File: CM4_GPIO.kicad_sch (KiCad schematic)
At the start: 13 parts, among them J10 Conn_01x03, J4 THD-20-R, J9 Conn_01x03, U12 SI-51005-F, U2 74LVC1G07SE-7

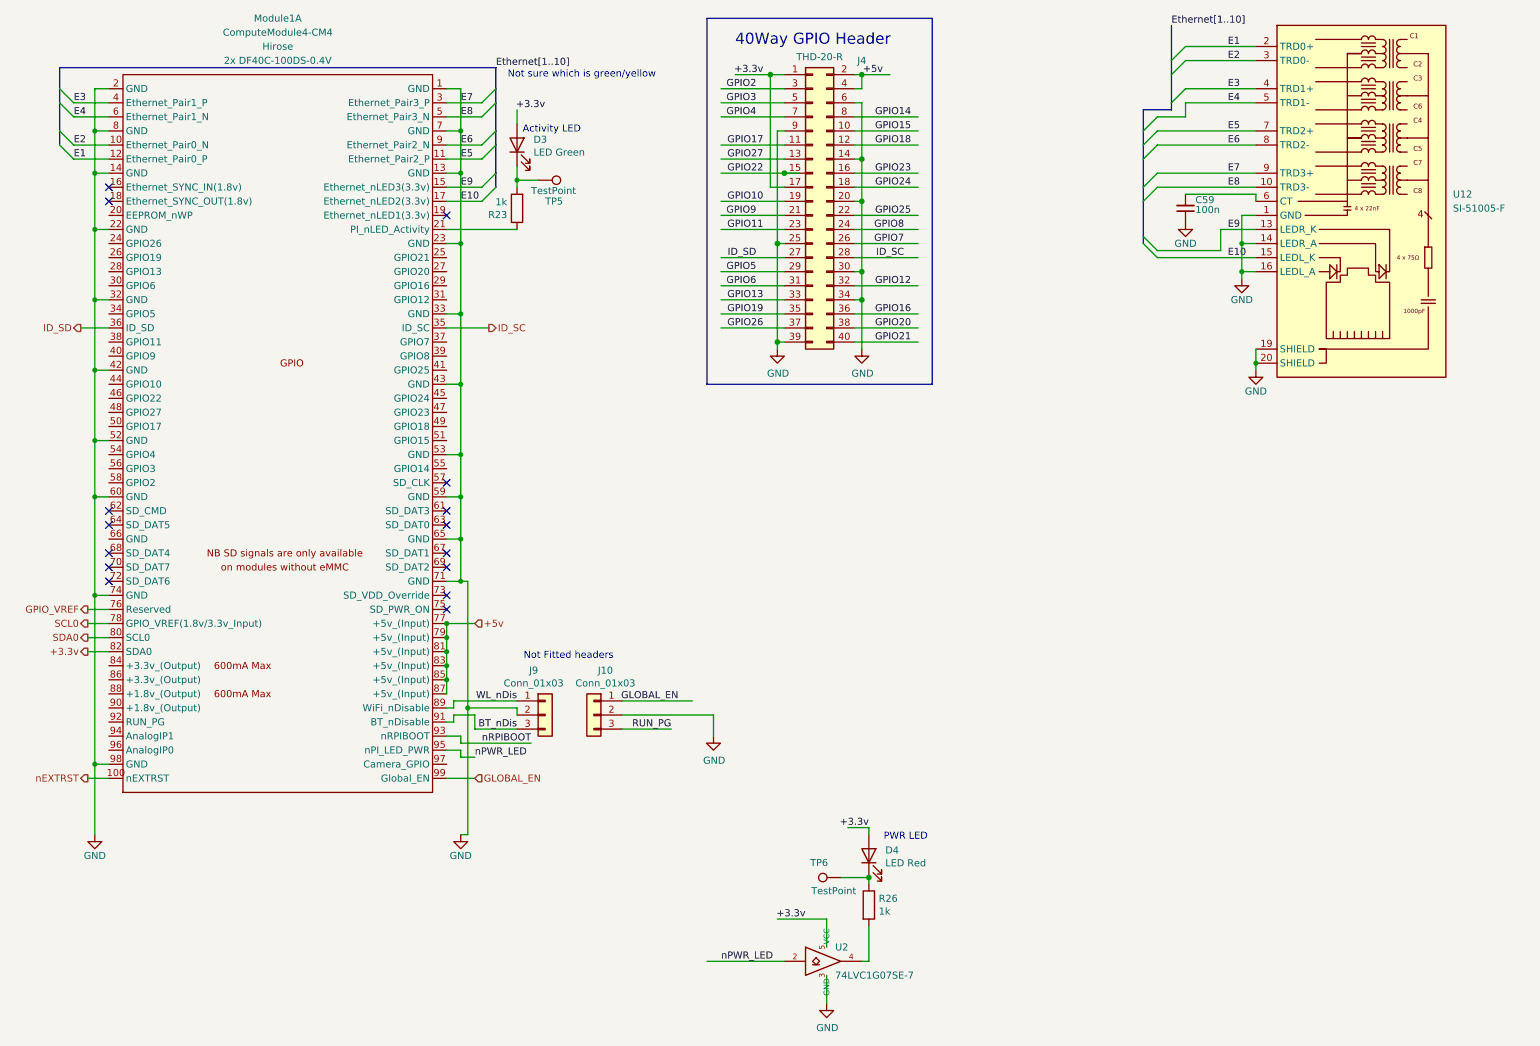
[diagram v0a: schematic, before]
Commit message: Heb mijn documentatie geleverd voor de USB-c en heb een BOM toegevoegd
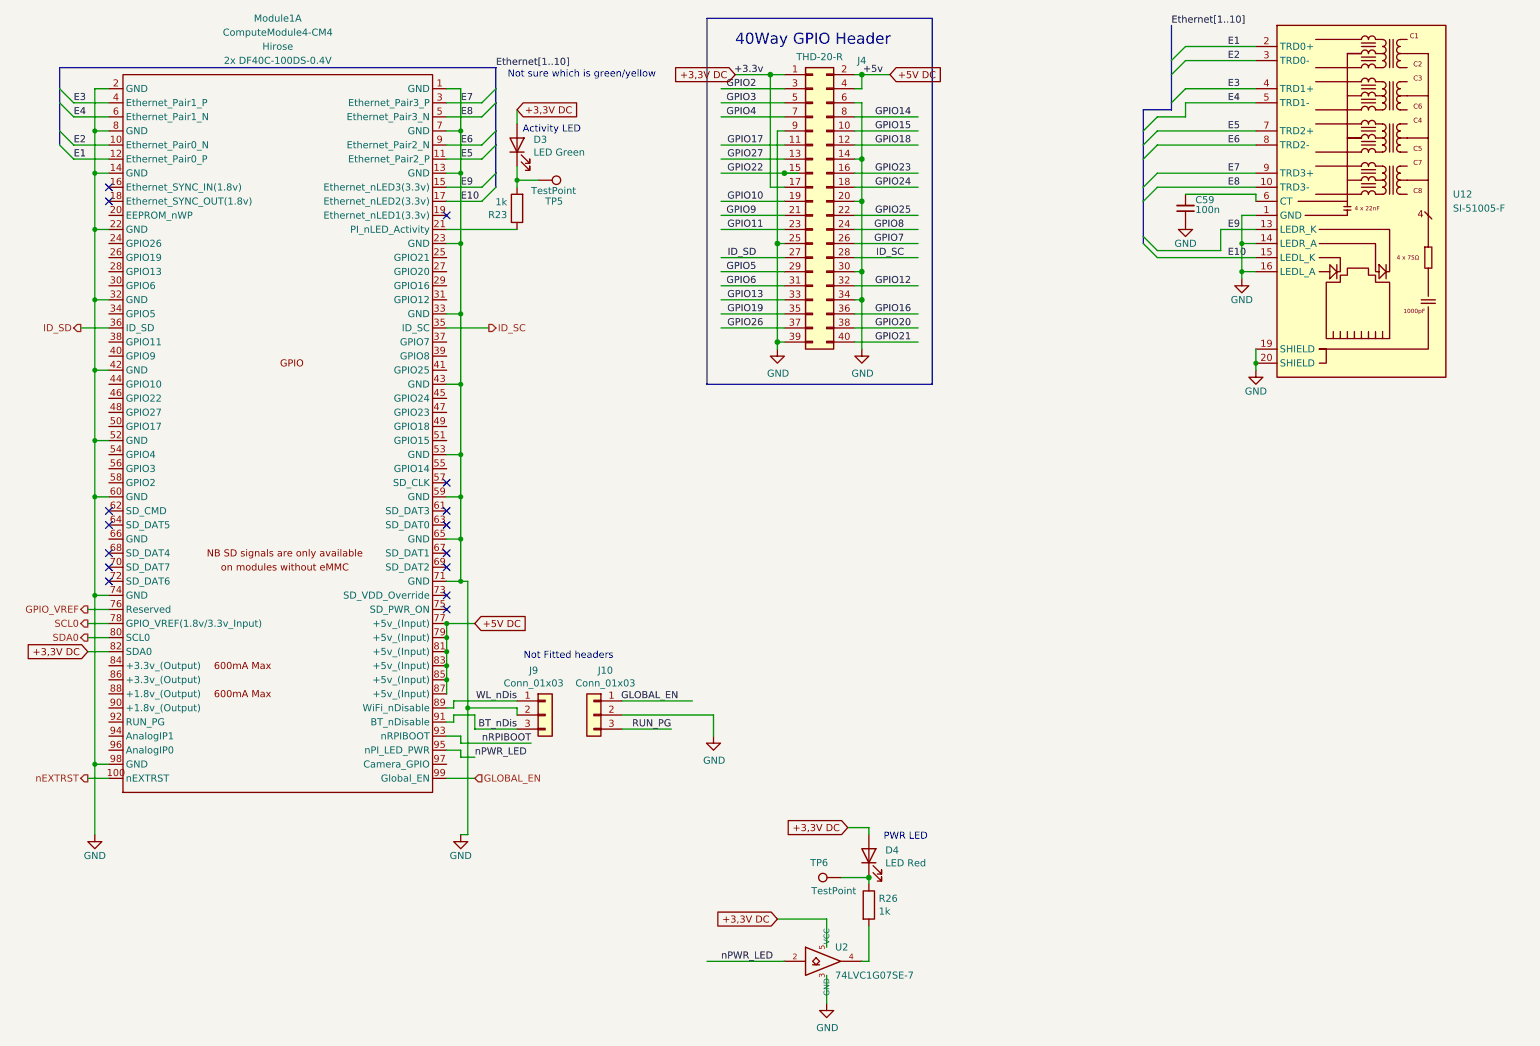
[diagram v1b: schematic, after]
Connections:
- net +3.3v is gone; now on net +3,3V DC: D4.2 (A), J4.1 (Pin_1), J4.17 (Pin_17), Module1.82 (SDA0), U2.5 (VCC)
- net +3,3V DC: now reaches D3.2 (A)
- net +5v renamed +5V DC
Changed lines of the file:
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@@
-		)
-	)
-	(label "+3.3v"
-		(at 153.67 176.53 180)
-		(effects
-			(font
-				(size 1.27 1.27)
-			)
-			(justify right bottom)
 		)
 	)
@@
 		)
 	)
-	(label "+3.3v"
-		(at 165.1 160.02 180)
-		(effects
-			(font
-				(size 1.27 1.27)
-			)
-			(justify right bottom)
-		)
-	)
 	(label "GPIO20"
 		(at 172.72 69.85 180)
@@
 		)
 	)
-	(label "+3.3v"
-		(at 106.68 30.48 180)
-		(effects
-			(font
-				(size 1.27 1.27)
-			)
-			(justify right bottom)
-		)
-	)
 	(label "E4"
 		(at 229.87 29.21 0)
@@
 			)
 			(justify right bottom)
+		)
+	)
+	(global_label "+5V DC"
+		(shape input)
+		(at 93.98 123.19 0)
+		(fields_autoplaced yes)
+		(effects
+			(font
+				(size 1.27 1.27)
+			)
+			(justify left)
+		)
+		(property "Intersheetrefs" "${INTERSHEET_REFS}"
+			(at 104.3433 123.19 0)
+			(effects
+				(font
+					(size 1.27 1.27)
+				)
+				(justify left)
+				(hide yes)
+			)
+		)
+	)
+	(global_label "+3,3V DC"
+		(shape input)
+		(at 161.29 160.02 180)
+		(fields_autoplaced yes)
+		(effects
+			(font
+				(size 1.27 1.27)
+			)
+			(justify right)
+		)
+		(property "Intersheetrefs" "${INTERSHEET_REFS}"
+			(at 149.1124 160.02 0)
+			(effects
+				(font
+					(size 1.27 1.27)
+				)
+				(justify right)
+				(hide yes)
+			)
+		)
+	)
+	(global_label "+3,3V DC"
+		(shape input)
+		(at 148.59 176.53 180)
+		(fields_autoplaced yes)
+		(effects
+			(font
+				(size 1.27 1.27)
+			)
+			(justify right)
+		)
+		(property "Intersheetrefs" "${INTERSHEET_REFS}"
+			(at 136.4124 176.53 0)
+			(effects
+				(font
+					(size 1.27 1.27)
+				)
+				(justify right)
+				(hide yes)
+			)
+		)
+	)
+	(global_label "+5V DC"
+		(shape input)
+		(at 168.91 24.13 0)
+		(fields_autoplaced yes)
+		(effects
+			(font
+				(size 1.27 1.27)
+			)
+			(justify left)
+		)
+		(property "Intersheetrefs" "${INTERSHEET_REFS}"
+			(at 179.2733 24.13 0)
+			(effects
+				(font
+					(size 1.27 1.27)
+				)
+				(justify left)
+				(hide yes)
+			)
+		)
+	)
+	(global_label "+3,3V DC"
+		(shape input)
+		(at 24.13 128.27 180)
+		(fields_autoplaced yes)
+		(effects
+			(font
+				(size 1.27 1.27)
+			)
+			(justify right)
+		)
+		(property "Intersheetrefs" "${INTERSHEET_REFS}"
+			(at 11.9524 128.27 0)
+			(effects
+				(font
+					(size 1.27 1.27)
+				)
+				(justify right)
+				(hide yes)
+			)
+		)
+	)
+	(global_label "+3,3V DC"
+		(shape input)
+		(at 140.97 24.13 180)
+		(fields_autoplaced yes)
+		(effects
+			(font
+				(size 1.27 1.27)
+			)
+			(justify right)
+		)
+		(property "Intersheetrefs" "${INTERSHEET_REFS}"
+			(at 128.7924 24.13 0)
+			(effects
+				(font
+					(size 1.27 1.27)
+				)
+				(justify right)
+				(hide yes)
+			)
+		)
+	)
+	(global_label "+3,3V DC"
+		(shape input)
+		(at 101.6 30.48 0)
+		(fields_autoplaced yes)
+		(effects
+			(font
+				(size 1.27 1.27)
+			)
+			(justify left)
+		)
+		(property "Intersheetrefs" "${INTERSHEET_REFS}"
+			(at 113.7776 30.48 0)
+			(effects
+				(font
+					(size 1.27 1.27)
+				)
+				(justify left)
+				(hide yes)
+			)
 		)
 	)
@@
 		)
 	)
-	(hierarchical_label "+3.3v"
-		(shape output)
-		(at 24.13 128.27 180)
-		(effects
-			(font
-				(size 1.27 1.27)
-			)
-			(justify right)
-		)
-	)
-	(hierarchical_label "+5v"
-		(shape input)
-		(at 93.98 123.19 0)
-		(effects
-			(font
-				(size 1.27 1.27)
-			)
-			(justify left)
-		)
-	)
